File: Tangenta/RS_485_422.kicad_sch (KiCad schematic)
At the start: 32 parts, among them J22 Conn_01x02_Pin, Q3 BSS138, U19 ADM2582E, U21 TPCDSOT23-SM712, U22 TPCDSOT23-SM712

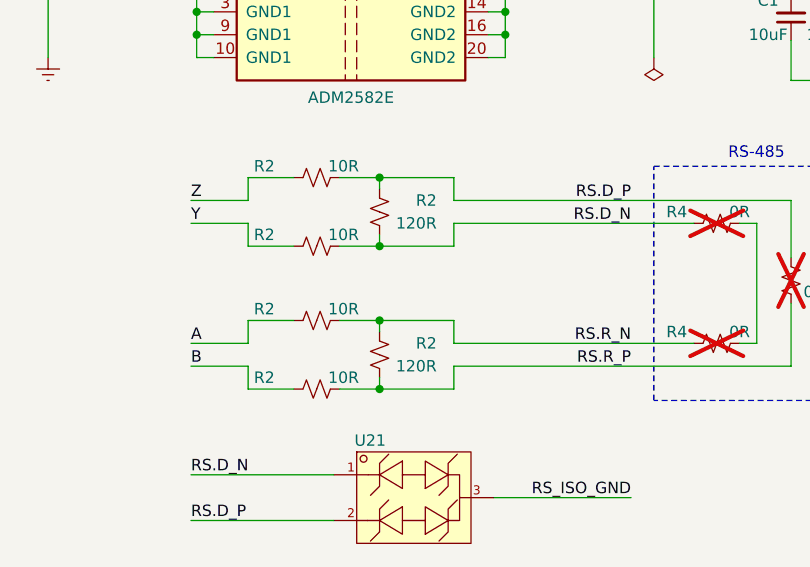
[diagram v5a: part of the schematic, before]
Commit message: CANbus current progress, RS-422 with 0603 termination resistor.
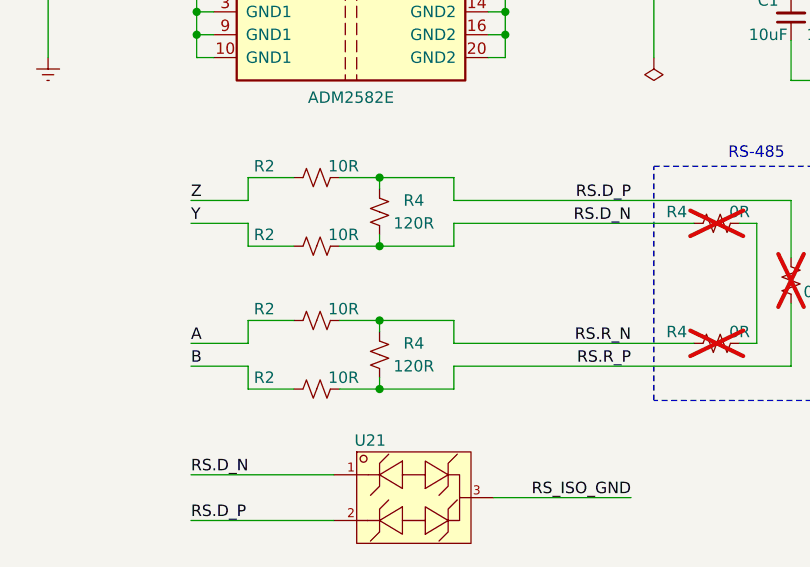
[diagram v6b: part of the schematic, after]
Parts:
- removed R2 (x2): 120R, Resistor_SMD:R_0402_1005Metric, symbol Device:R_Small_US
- added R4 (x2): 120R, Resistor_SMD:R_0603_1608Metric, symbol Device:R_Small_US
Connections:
- net RS.D_N: now also R4.2
- net RS.D_P: now also R4.1
- net RS.R_N: now also R4.2
- net RS.R_P: now also R4.1
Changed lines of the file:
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@@
-    )
-  )
-  (symbol (lib_id "Device:R_Small_US") (at 213.36 95.25 180) (unit 1)
-    (in_bom yes) (on_board yes) (dnp no)
-    (property "Reference" "R2" (at 219.71 93.98 0)
-      (effects (font (size 1.27 1.27)) (justify left))
-    )
-    (property "Value" "120R" (at 219.71 96.52 0)
-      (effects (font (size 1.27 1.27)) (justify left))
-    )
-    (property "Footprint" "Resistor_SMD:R_0402_1005Metric" (at 213.36 95.25 0)
-      (effects (font (size 1.27 1.27)) hide)
-    )
-    (property "Datasheet" "~" (at 213.36 95.25 0)
-      (effects (font (size 1.27 1.27)) hide)
-    )
-    (pin "1")
-    (pin "2")
-    (instances
-      (project "Tangenta"
-        (path "/358d1bcf-7599-4352-8c4d-baa18a5f09e6/8215796b-9611-4f43-bcc5-319f8414b8a6"
-          (reference "R2") (unit 1)
-        )
-        (path "/358d1bcf-7599-4352-8c4d-baa18a5f09e6/d6c05402-162e-441f-bed8-be7996260fb4"
-          (reference "R18") (unit 1)
-        )
-        (path "/358d1bcf-7599-4352-8c4d-baa18a5f09e6/b1871a4d-6a35-44e2-a9a2-9a4af684371d"
-          (reference "R26") (unit 1)
-        )
-        (path "/358d1bcf-7599-4352-8c4d-baa18a5f09e6/6a8c68b5-4a7d-449e-86f6-34ced6d1cb55"
-          (reference "R41") (unit 1)
-        )
-        (path "/358d1bcf-7599-4352-8c4d-baa18a5f09e6/db297b0b-35f2-4e86-892c-83973f1ac2db"
-          (reference "R41") (unit 1)
-        )
-        (path "/358d1bcf-7599-4352-8c4d-baa18a5f09e6/98e3b24f-9927-4339-b8fd-9deea91a522a"
-          (reference "R168") (unit 1)
-        )
-      )
     )
   )
@@
     )
   )
+  (symbol (lib_id "Device:R_Small_US") (at 213.36 79.375 0) (unit 1)
+    (in_bom yes) (on_board yes) (dnp no)
+    (property "Reference" "R4" (at 217.17 78.105 0)
+      (effects (font (size 1.27 1.27)))
+    )
+    (property "Value" "120R" (at 217.17 80.645 0)
+      (effects (font (size 1.27 1.27)))
+    )
+    (property "Footprint" "Resistor_SMD:R_0603_1608Metric" (at 213.36 79.375 0)
+      (effects (font (size 1.27 1.27)) hide)
+    )
+    (property "Datasheet" "~" (at 213.36 79.375 0)
+      (effects (font (size 1.27 1.27)) hide)
+    )
+    (pin "1")
+    (pin "2")
+    (instances
+      (project "Tangenta"
+        (path "/358d1bcf-7599-4352-8c4d-baa18a5f09e6/8215796b-9611-4f43-bcc5-319f8414b8a6"
+          (reference "R4") (unit 1)
+        )
+        (path "/358d1bcf-7599-4352-8c4d-baa18a5f09e6/98e3b24f-9927-4339-b8fd-9deea91a522a"
+          (reference "R182") (unit 1)
+        )
+      )
+    )
+  )
   (symbol (lib_id "Device:C_Small") (at 266.7 36.195 180) (unit 1)
     (in_bom yes) (on_board yes) (dnp no)
@@
         (path "/358d1bcf-7599-4352-8c4d-baa18a5f09e6/98e3b24f-9927-4339-b8fd-9deea91a522a"
           (reference "C181") (unit 1)
-        )
-      )
-    )
-  )
-  (symbol (lib_id "Device:R_Small_US") (at 213.36 79.375 180) (unit 1)
-    (in_bom yes) (on_board yes) (dnp no)
-    (property "Reference" "R2" (at 219.71 78.105 0)
-      (effects (font (size 1.27 1.27)) (justify left))
-    )
-    (property "Value" "120R" (at 219.71 80.645 0)
-      (effects (font (size 1.27 1.27)) (justify left))
-    )
-    (property "Footprint" "Resistor_SMD:R_0402_1005Metric" (at 213.36 79.375 0)
-      (effects (font (size 1.27 1.27)) hide)
-    )
-    (property "Datasheet" "~" (at 213.36 79.375 0)
-      (effects (font (size 1.27 1.27)) hide)
-    )
-    (pin "1")
-    (pin "2")
-    (instances
-      (project "Tangenta"
-        (path "/358d1bcf-7599-4352-8c4d-baa18a5f09e6/8215796b-9611-4f43-bcc5-319f8414b8a6"
-          (reference "R2") (unit 1)
-        )
-        (path "/358d1bcf-7599-4352-8c4d-baa18a5f09e6/d6c05402-162e-441f-bed8-be7996260fb4"
-          (reference "R18") (unit 1)
-        )
-        (path "/358d1bcf-7599-4352-8c4d-baa18a5f09e6/b1871a4d-6a35-44e2-a9a2-9a4af684371d"
-          (reference "R26") (unit 1)
-        )
-        (path "/358d1bcf-7599-4352-8c4d-baa18a5f09e6/6a8c68b5-4a7d-449e-86f6-34ced6d1cb55"
-          (reference "R41") (unit 1)
-        )
-        (path "/358d1bcf-7599-4352-8c4d-baa18a5f09e6/db297b0b-35f2-4e86-892c-83973f1ac2db"
-          (reference "R41") (unit 1)
-        )
-        (path "/358d1bcf-7599-4352-8c4d-baa18a5f09e6/98e3b24f-9927-4339-b8fd-9deea91a522a"
-          (reference "R151") (unit 1)
         )
       )
@@
         )
       )
+    )
+  )
+  (symbol (lib_id "Device:R_Small_US") (at 213.36 95.25 180) (unit 1)
+    (in_bom yes) (on_board yes) (dnp no)
+    (property "Reference" "R4" (at 217.17 93.98 0)
+      (effects (font (size 1.27 1.27)))
+    )
+    (property "Value" "120R" (at 217.17 96.52 0)
+      (effects (font (size 1.27 1.27)))
+    )
+    (property "Footprint" "Resistor_SMD:R_0603_1608Metric" (at 213.36 95.25 0)
+      (effects (font (size 1.27 1.27)) hide)
+    )
+    (property "Datasheet" "~" (at 213.36 95.25 0)
+      (effects (font (size 1.27 1.27)) hide)
+    )
+    (pin "1")
+    (pin "2")
+    (instances
+      (project "Tangenta"
+        (path "/358d1bcf-7599-4352-8c4d-baa18a5f09e6/8215796b-9611-4f43-bcc5-319f8414b8a6"
+          (reference "R4") (unit 1)
+        )
+        (path "/358d1bcf-7599-4352-8c4d-baa18a5f09e6/98e3b24f-9927-4339-b8fd-9deea91a522a"
+          (reference "R183") (unit 1)
+        )
+      )

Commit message: Libraries exported from global to project.
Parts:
- C1: symbol Device:C_Small -> CholaSymbolsPrjLib:C_Small
- C178: symbol CAP_L5:16CE47FSS -> CholaSymbolsPrjLib:16CE47FSS
- J22: symbol Connector:Conn_01x02_Pin -> CholaSymbolsPrjLib:Conn_01x02_Pin
- Q3: symbol Transistor_FET:BSS138 -> CholaSymbolsPrjLib:BSS138
- R2, R4: symbol Device:R_Small_US -> CholaSymbolsPrjLib:R_Small_US
- U19: symbol Interface_UART:ADM2582E -> CholaSymbolsPrjLib:ADM2582E
- U21, U22: symbol ESD_RS485:TPCDSOT23-SM712 -> CholaSymbolsPrjLib:TPCDSOT23-SM712
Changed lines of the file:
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@@
     )
   )
-  (symbol (lib_id "Device:R_Small_US") (at 137.795 40.64 180) (unit 1)
+  (symbol (lib_id "CholaSymbolsPrjLib:R_Small_US") (at 137.795 40.64 180) (unit 1)
     (in_bom yes) (on_board yes) (dnp no)
     (property "Reference" "R2" (at 136.525 39.37 0)
@@
     )
   )
-  (symbol (lib_id "Device:R_Small_US") (at 206.375 75.565 270) (unit 1)
+  (symbol (lib_id "CholaSymbolsPrjLib:R_Small_US") (at 206.375 75.565 270) (unit 1)
     (in_bom yes) (on_board yes) (dnp no)
     (property "Reference" "R2" (at 199.39 74.295 90)
@@
     )
   )
-  (symbol (lib_id "Device:R_Small_US") (at 250.825 80.645 270) (unit 1)
+  (symbol (lib_id "CholaSymbolsPrjLib:R_Small_US") (at 250.825 80.645 270) (unit 1)
     (in_bom no) (on_board yes) (dnp yes)
     (property "Reference" "R4" (at 246.38 79.375 90)
@@
     )
   )
-  (symbol (lib_id "Device:R_Small_US") (at 137.795 82.55 180) (unit 1)
+  (symbol (lib_id "CholaSymbolsPrjLib:R_Small_US") (at 137.795 82.55 180) (unit 1)
     (in_bom yes) (on_board yes) (dnp no)
     (property "Reference" "R2" (at 136.525 81.28 0)
@@
     )
   )
-  (symbol (lib_id "Device:R_Small_US") (at 206.375 91.44 270) (unit 1)
+  (symbol (lib_id "CholaSymbolsPrjLib:R_Small_US") (at 206.375 91.44 270) (unit 1)
     (in_bom yes) (on_board yes) (dnp no)
     (property "Reference" "R2" (at 199.39 90.17 90)
@@
     )
   )
-  (symbol (lib_id "Device:R_Small_US") (at 213.36 79.375 0) (unit 1)
+  (symbol (lib_id "CholaSymbolsPrjLib:R_Small_US") (at 213.36 79.375 0) (unit 1)
     (in_bom yes) (on_board yes) (dnp no)
     (property "Reference" "R4" (at 217.17 78.105 0)
@@
     )
   )
-  (symbol (lib_id "Device:C_Small") (at 266.7 36.195 180) (unit 1)
+  (symbol (lib_id "CholaSymbolsPrjLib:C_Small") (at 266.7 36.195 180) (unit 1)
     (in_bom yes) (on_board yes) (dnp no)
     (property "Reference" "C1" (at 264.1599 34.2899 0)
@@
     )
   )
-  (symbol (lib_id "Transistor_FET:BSS138") (at 123.825 65.405 270) (unit 1)
+  (symbol (lib_id "CholaSymbolsPrjLib:BSS138") (at 123.825 65.405 270) (unit 1)
     (in_bom yes) (on_board yes) (dnp no)
     (property "Reference" "Q3" (at 126.365 62.865 90)
@@
     )
   )
-  (symbol (lib_id "Device:R_Small_US") (at 206.375 99.06 270) (unit 1)
+  (symbol (lib_id "CholaSymbolsPrjLib:R_Small_US") (at 206.375 99.06 270) (unit 1)
     (in_bom yes) (on_board yes) (dnp no)
     (property "Reference" "R2" (at 199.39 97.79 90)
@@
     )
   )
-  (symbol (lib_id "Device:R_Small_US") (at 259.08 86.995 0) (unit 1)
+  (symbol (lib_id "CholaSymbolsPrjLib:R_Small_US") (at 259.08 86.995 0) (unit 1)
     (in_bom no) (on_board yes) (dnp yes)
     (property "Reference" "R4" (at 262.89 86.36 0)
@@
     )
   )
-  (symbol (lib_id "Device:C_Small") (at 266.7 57.785 180) (unit 1)
+  (symbol (lib_id "CholaSymbolsPrjLib:C_Small") (at 266.7 57.785 180) (unit 1)
     (in_bom yes) (on_board yes) (dnp no)
     (property "Reference" "C1" (at 264.1599 55.8799 0)
@@
     )
   )
-  (symbol (lib_id "Device:R_Small_US") (at 206.375 83.185 270) (unit 1)
+  (symbol (lib_id "CholaSymbolsPrjLib:R_Small_US") (at 206.375 83.185 270) (unit 1)
     (in_bom yes) (on_board yes) (dnp no)
     (property "Reference" "R2" (at 199.39 81.915 90)
@@
     )
   )
-  (symbol (lib_id "Device:C_Small") (at 259.08 36.195 180) (unit 1)
+  (symbol (lib_id "CholaSymbolsPrjLib:C_Small") (at 259.08 36.195 180) (unit 1)
     (in_bom yes) (on_board yes) (dnp no)
     (property "Reference" "C1" (at 256.5399 34.2899 0)
@@
     )
   )
-  (symbol (lib_id "Device:R_Small_US") (at 137.795 61.595 180) (unit 1)
+  (symbol (lib_id "CholaSymbolsPrjLib:R_Small_US") (at 137.795 61.595 180) (unit 1)
     (in_bom yes) (on_board yes) (dnp no)
     (property "Reference" "R2" (at 136.525 60.325 0)
@@
     )
   )
-  (symbol (lib_id "Transistor_FET:BSS138") (at 123.825 44.45 270) (unit 1)
+  (symbol (lib_id "CholaSymbolsPrjLib:BSS138") (at 123.825 44.45 270) (unit 1)
     (in_bom yes) (on_board yes) (dnp no)
     (property "Reference" "Q3" (at 126.365 41.91 90)
@@
     )
   )
-  (symbol (lib_id "CAP_L5:16CE47FSS") (at 48.26 47.625 0) (unit 1)
+  (symbol (lib_id "CholaSymbolsPrjLib:16CE47FSS") (at 48.26 47.625 0) (unit 1)
     (in_bom yes) (on_board yes) (dnp no)
     (property "Reference" "C178" (at 49.53 45.72 0)
@@
     )
   )
-  (symbol (lib_id "Device:R_Small_US") (at 111.125 82.55 180) (unit 1)
+  (symbol (lib_id "CholaSymbolsPrjLib:R_Small_US") (at 111.125 82.55 180) (unit 1)
     (in_bom yes) (on_board yes) (dnp no)
     (property "Reference" "R2" (at 109.855 81.28 0)
@@
     )
   )
-  (symbol (lib_id "Device:R_Small_US") (at 111.125 103.505 180) (unit 1)
+  (symbol (lib_id "CholaSymbolsPrjLib:R_Small_US") (at 111.125 103.505 180) (unit 1)
     (in_bom yes) (on_board yes) (dnp no)
     (property "Reference" "R2" (at 109.855 102.235 0)
@@
     )
   )
-  (symbol (lib_id "ESD_RS485:TPCDSOT23-SM712") (at 216.916 127.635 0) (unit 1)
+  (symbol (lib_id "CholaSymbolsPrjLib:TPCDSOT23-SM712") (at 216.916 127.635 0) (unit 1)
     (in_bom yes) (on_board yes) (dnp no)
     (property "Reference" "U22" (at 210.566 121.285 0)
@@
     )
   )
-  (symbol (lib_id "Device:R_Small_US") (at 111.125 40.64 180) (unit 1)
+  (symbol (lib_id "CholaSymbolsPrjLib:R_Small_US") (at 111.125 40.64 180) (unit 1)
     (in_bom yes) (on_board yes) (dnp no)
     (property "Reference" "R2" (at 109.855 39.37 0)
@@
     )
   )
-  (symbol (lib_id "Device:C_Small") (at 274.32 57.785 180) (unit 1)
+  (symbol (lib_id "CholaSymbolsPrjLib:C_Small") (at 274.32 57.785 180) (unit 1)
     (in_bom yes) (on_board yes) (dnp no)
     (property "Reference" "C1" (at 271.7799 55.8799 0)
@@
     )
   )
-  (symbol (lib_id "Transistor_FET:BSS138") (at 123.825 86.36 270) (unit 1)
+  (symbol (lib_id "CholaSymbolsPrjLib:BSS138") (at 123.825 86.36 270) (unit 1)
     (in_bom yes) (on_board yes) (dnp no)
     (property "Reference" "Q3" (at 126.365 83.82 90)
@@
     )
   )
-  (symbol (lib_id "Interface_UART:ADM2582E") (at 210.185 49.53 0) (unit 1)
+  (symbol (lib_id "CholaSymbolsPrjLib:ADM2582E") (at 210.185 49.53 0) (unit 1)
     (in_bom yes) (on_board yes) (dnp no)
     (property "Reference" "U19" (at 210.185 30.48 0)
@@
     )
   )
-  (symbol (lib_id "Device:R_Small_US") (at 137.795 103.505 180) (unit 1)
+  (symbol (lib_id "CholaSymbolsPrjLib:R_Small_US") (at 137.795 103.505 180) (unit 1)
     (in_bom yes) (on_board yes) (dnp no)
     (property "Reference" "R2" (at 136.525 102.235 0)
@@
     )
   )
-  (symbol (lib_id "Transistor_FET:BSS138") (at 123.825 107.315 270) (unit 1)
+  (symbol (lib_id "CholaSymbolsPrjLib:BSS138") (at 123.825 107.315 270) (unit 1)
     (in_bom yes) (on_board yes) (dnp no)
     (property "Reference" "Q3" (at 126.365 104.775 90)
@@
     )
   )
-  (symbol (lib_id "Device:C_Small") (at 274.32 36.195 180) (unit 1)
+  (symbol (lib_id "CholaSymbolsPrjLib:C_Small") (at 274.32 36.195 180) (unit 1)
     (in_bom yes) (on_board yes) (dnp no)
     (property "Reference" "C1" (at 271.7799 34.2899 0)
@@
     )
   )
-  (symbol (lib_id "Device:R_Small_US") (at 111.125 61.595 180) (unit 1)
+  (symbol (lib_id "CholaSymbolsPrjLib:R_Small_US") (at 111.125 61.595 180) (unit 1)
     (in_bom yes) (on_board yes) (dnp no)
     (property "Reference" "R2" (at 109.855 60.325 0)
@@
     )
   )
-  (symbol (lib_id "Device:R_Small_US") (at 250.825 93.98 270) (unit 1)
+  (symbol (lib_id "CholaSymbolsPrjLib:R_Small_US") (at 250.825 93.98 270) (unit 1)
     (in_bom no) (on_board yes) (dnp yes)
     (property "Reference" "R4" (at 246.38 92.71 90)
@@
     )
   )
-  (symbol (lib_id "Connector:Conn_01x02_Pin") (at 198.12 154.94 270) (unit 1)
+  (symbol (lib_id "CholaSymbolsPrjLib:Conn_01x02_Pin") (at 198.12 154.94 270) (unit 1)
     (in_bom yes) (on_board yes) (dnp no)
     (property "Reference" "J22" (at 194.945 153.67 90)
@@
     )
   )
-  (symbol (lib_id "Device:R_Small_US") (at 213.36 95.25 180) (unit 1)
+  (symbol (lib_id "CholaSymbolsPrjLib:R_Small_US") (at 213.36 95.25 180) (unit 1)
     (in_bom yes) (on_board yes) (dnp no)
     (property "Reference" "R4" (at 217.17 93.98 0)
@@
     )
   )
-  (symbol (lib_id "ESD_RS485:TPCDSOT23-SM712") (at 216.916 111.125 0) (unit 1)
+  (symbol (lib_id "CholaSymbolsPrjLib:TPCDSOT23-SM712") (at 216.916 111.125 0) (unit 1)
     (in_bom yes) (on_board yes) (dnp no)
     (property "Reference" "U21" (at 210.566 104.775 0)
@@
     )
   )
-  (symbol (lib_id "Device:C_Small") (at 259.08 57.785 180) (unit 1)
+  (symbol (lib_id "CholaSymbolsPrjLib:C_Small") (at 259.08 57.785 180) (unit 1)
     (in_bom yes) (on_board yes) (dnp no)
     (property "Reference" "C1" (at 256.5399 55.8799 0)
